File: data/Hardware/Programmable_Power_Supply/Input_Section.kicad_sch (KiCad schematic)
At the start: 20 parts, among them J1 Barrel_Jack_MountingPin, Q1 BSC050N03LS_G, Q2 2N7002, U2 TPS26631PWP, U3 TPS54202DDC

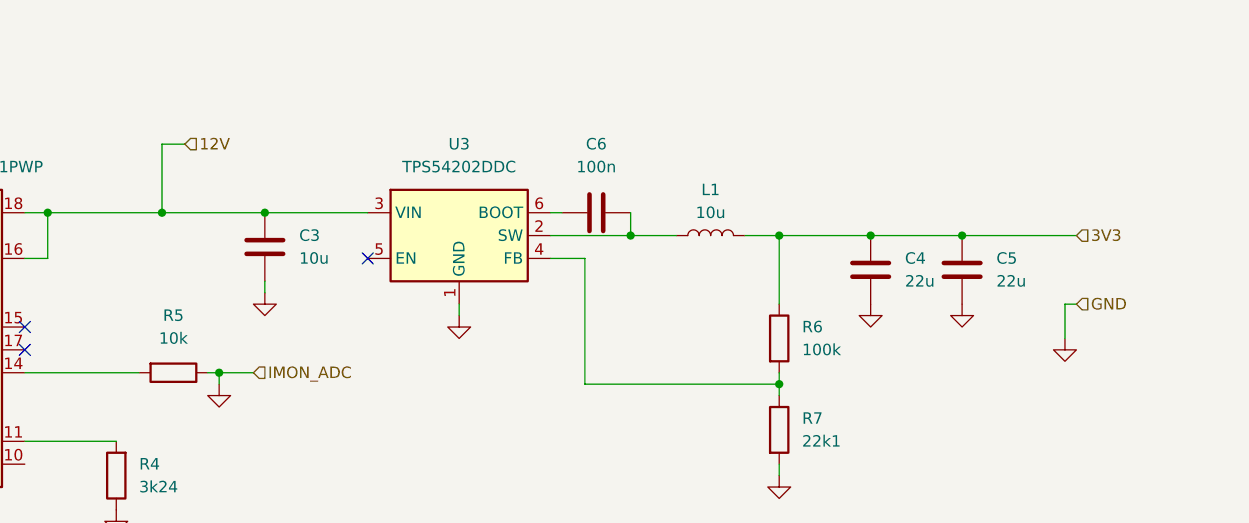
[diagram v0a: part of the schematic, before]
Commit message: feat: Adding output section to the schematic.
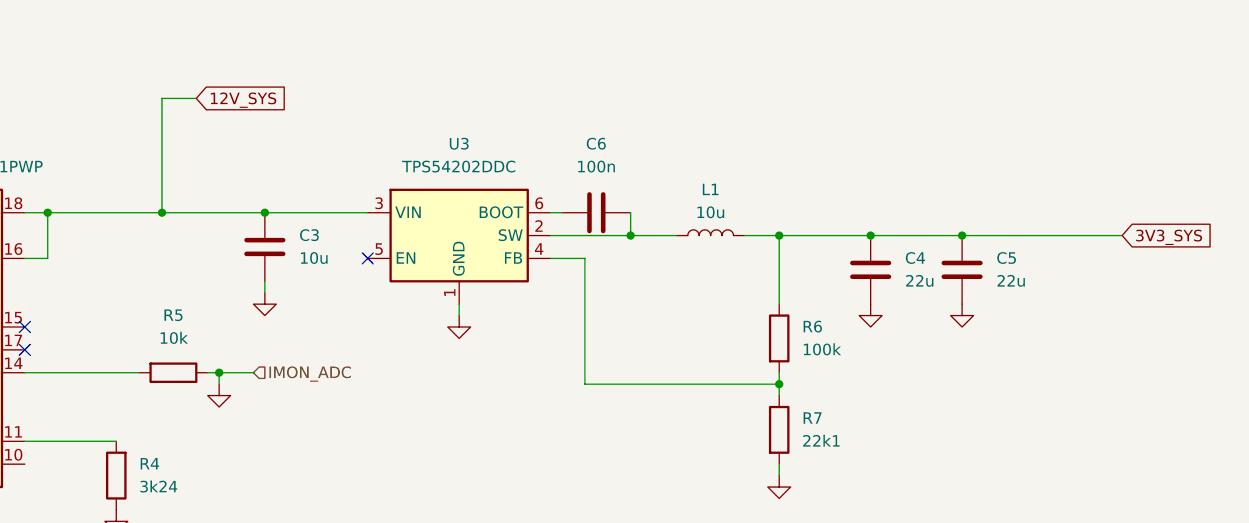
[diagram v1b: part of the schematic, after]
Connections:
- net 12V renamed 12V_SYS
- net 3V3 renamed 3V3_SYS
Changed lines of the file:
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@@
+	(wire
+		(pts
+			(xy 151.13 50.8) (xy 154.94 50.8)
+		)
+		(stroke
+			(width 0)
+			(type default)
+		)
+	)
 	(wire
 		(pts
@@
 	(wire
 		(pts
-			(xy 251.46 73.66) (xy 251.46 77.47)
-		)
-		(stroke
-			(width 0)
-			(type default)
-		)
-	)
-	(wire
-		(pts
 			(xy 63.5 49.53) (xy 76.2 49.53)
 		)
@@
 	(wire
 		(pts
-			(xy 153.67 55.88) (xy 151.13 55.88)
-		)
-		(stroke
-			(width 0)
-			(type default)
-		)
-	)
-	(wire
-		(pts
 			(xy 198.12 82.55) (xy 219.71 82.55)
 		)
@@
 	(wire
 		(pts
-			(xy 240.03 66.04) (xy 252.73 66.04)
+			(xy 240.03 66.04) (xy 257.81 66.04)
 		)
 		(stroke
@@
 	(wire
 		(pts
-			(xy 151.13 55.88) (xy 151.13 63.5)
-		)
-		(stroke
-			(width 0)
-			(type default)
-		)
-	)
-	(wire
-		(pts
 			(xy 76.2 83.82) (xy 76.2 90.17)
 		)
@@
 	(wire
 		(pts
-			(xy 252.73 73.66) (xy 251.46 73.66)
-		)
-		(stroke
-			(width 0)
-			(type default)
-		)
-	)
-	(wire
-		(pts
 			(xy 53.34 49.53) (xy 63.5 49.53)
 		)
@@
 	(wire
 		(pts
+			(xy 151.13 50.8) (xy 151.13 63.5)
+		)
+		(stroke
+			(width 0)
+			(type default)
+		)
+	)
+	(wire
+		(pts
 			(xy 88.9 83.82) (xy 76.2 83.82)
 		)
@@
 		)
 	)
-	(hierarchical_label "12V"
+	(global_label "3V3_SYS"
 		(shape input)
-		(at 153.67 55.88 0)
+		(at 257.81 66.04 0)
+		(fields_autoplaced yes)
 		(effects
 			(font
@@
 			(justify left)
 		)
-	)
-	(hierarchical_label "GND"
+		(property "Intersheetrefs" "${INTERSHEET_REFS}"
+			(at 268.778 66.04 0)
+			(effects
+				(font
+					(size 1.27 1.27)
+				)
+				(justify left)
+				(hide yes)
+			)
+		)
+	)
+	(global_label "12V_SYS"
 		(shape input)
-		(at 252.73 73.66 0)
+		(at 154.94 50.8 0)
+		(fields_autoplaced yes)
 		(effects
 			(font
@@
 			)
 			(justify left)
+		)
+		(property "Intersheetrefs" "${INTERSHEET_REFS}"
+			(at 165.908 50.8 0)
+			(effects
+				(font
+					(size 1.27 1.27)
+				)
+				(justify left)
+				(hide yes)
+			)
 		)
 	)
@@
 		)
 	)
-	(hierarchical_label "3V3"
-		(shape input)
-		(at 252.73 66.04 0)
-		(effects
-			(font
-				(size 1.27 1.27)
-			)
-			(justify left)
-		)
-	)
 	(symbol
 		(lib_id "power:GND")
@@
 					(unit 1)
 				)
-			)
-		)
-	)
-	(symbol
-		(lib_id "power:GND")
-		(at 251.46 77.47 0)
-		(unit 1)
-		(exclude_from_sim no)
-		(in_bom yes)
-		(on_board yes)
-		(dnp no)
-		(fields_autoplaced yes)
-		(property "Reference" "#PWR03"
-			(at 251.46 83.82 0)
-			(effects
-				(font
-					(size 1.27 1.27)
-				)
-				(hide yes)
-			)
-		)
-		(property "Value" "GND"
-			(at 251.46 82.55 0)
-			(effects
-				(font
-					(size 1.27 1.27)
-				)
-				(hide yes)
-			)
-		)
-		(property "Footprint" ""
-			(at 251.46 77.47 0)
-			(effects
-				(font
-					(size 1.27 1.27)
-				)
-				(hide yes)
-			)
-		)
-		(property "Datasheet" ""
-			(at 251.46 77.47 0)
-			(effects
-				(font
-					(size 1.27 1.27)
-				)
-				(hide yes)
-			)
-		)
-		(property "Description" "Power symbol creates a global label with name \"GND\" , ground"
-			(at 251.46 77.47 0)
-			(effects
-				(font
-					(size 1.27 1.27)
-				)
-				(hide yes)
-			)
-		)
-		(pin "1"
-		)
-		(instances
-			(project "Programmable_Power_Supply"
-				(path "/b54e5edd-9bd1-4c5e-a8c2-662f0aedeac0/0d4dc9d8-4ae1-4f7b-b0fe-cdea114c506b"
-					(reference "#PWR03")
-					(unit 1)
-				)

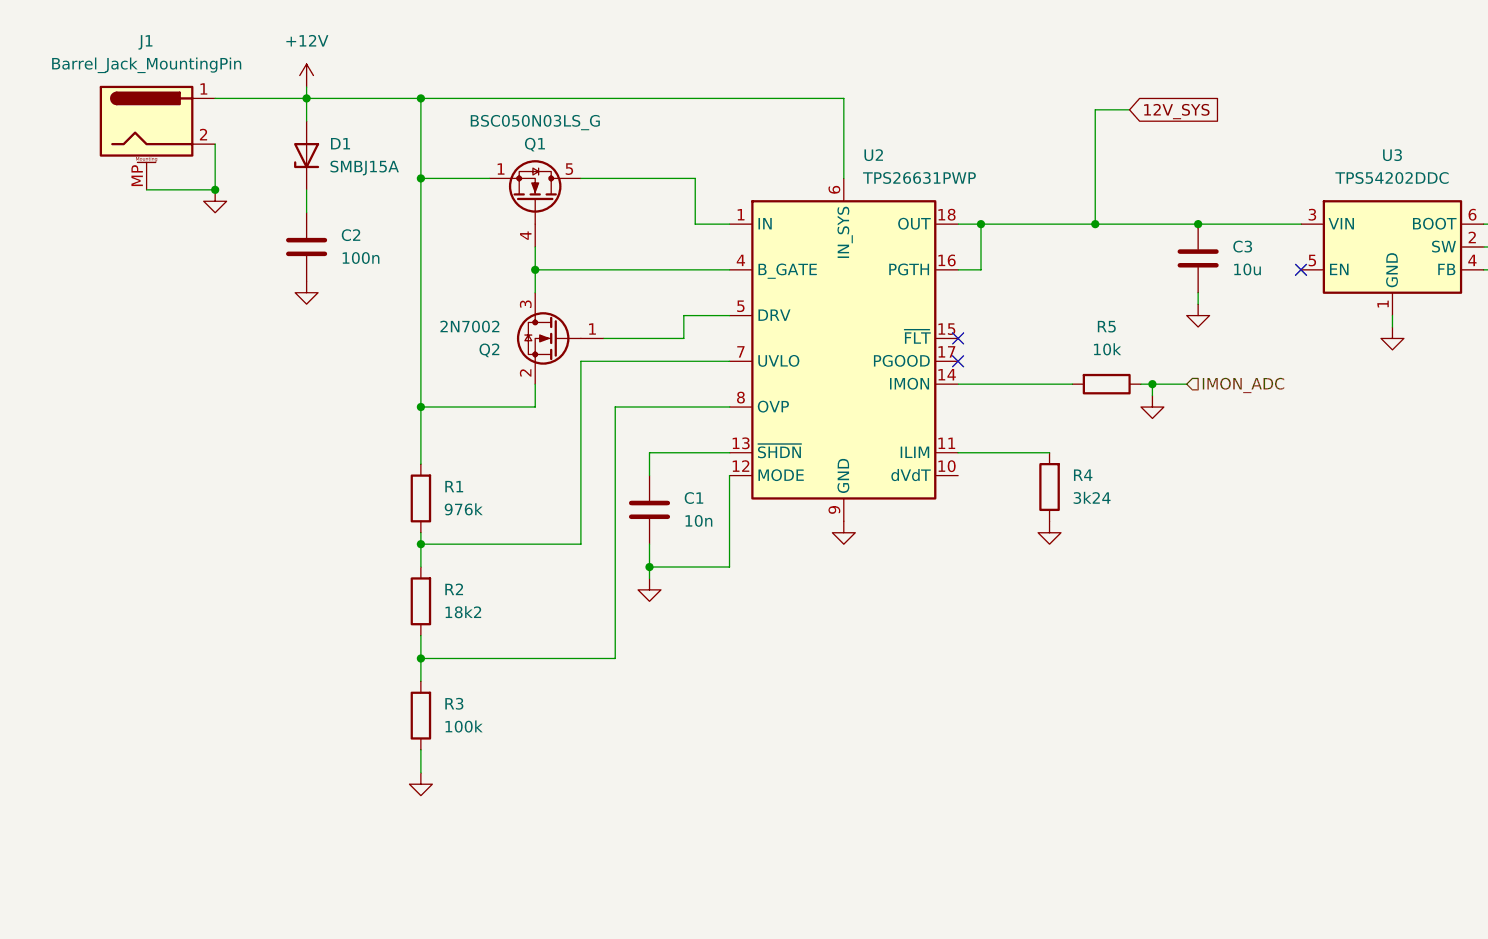
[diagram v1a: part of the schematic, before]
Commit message: feat: First draw of full schematic with all footprints and symbols.
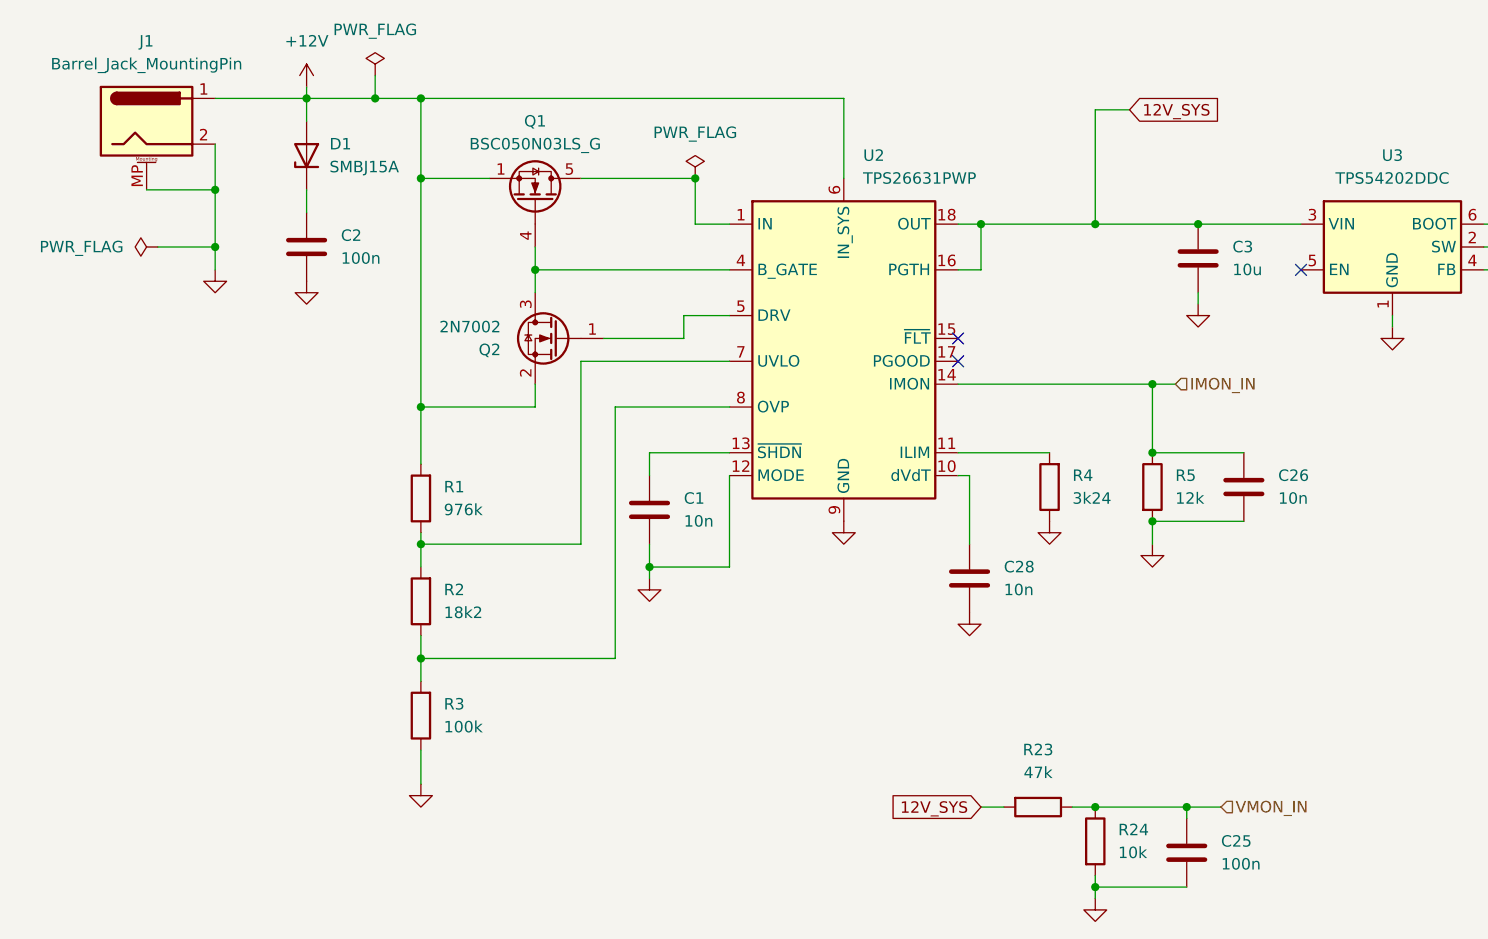
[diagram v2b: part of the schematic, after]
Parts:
- added C25: 100n, Capacitor_SMD:C_0805_2012Metric_Pad1.18x1.45mm_HandSolder, symbol Device:C
- added C26, C28: 10n, Capacitor_SMD:C_0805_2012Metric_Pad1.18x1.45mm_HandSolder, symbol Device:C
- added R23: 47k, Resistor_SMD:R_0603_1608Metric_Pad0.98x0.95mm_HandSolder, symbol Device:R
- added R24: 10k, Resistor_SMD:R_0603_1608Metric_Pad0.98x0.95mm_HandSolder, symbol Device:R
- C1: footprint (none) -> Capacitor_SMD:C_0201_0603Metric_Pad0.64x0.40mm_HandSolder
- C2, C6: footprint (none) -> Capacitor_SMD:C_0805_2012Metric_Pad1.18x1.45mm_HandSolder
- C3, C4, C5: footprint (none) -> Capacitor_SMD:C_1206_3216Metric_Pad1.33x1.80mm_HandSolder
- L1: footprint (none) -> Inductor_SMD:L_Taiyo-Yuden_NR-60xx_HandSoldering
- R1, R2, R3, R4, R6, R7: footprint (none) -> Resistor_SMD:R_0603_1608Metric_Pad0.98x0.95mm_HandSolder
- R5: value 10k -> 12k; footprint (none) -> Resistor_SMD:R_0603_1608Metric_Pad0.98x0.95mm_HandSolder
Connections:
- net +12V: now also Q1.2 (S), Q1.3 (S)
- net 12V_SYS: now also R23.2
- net GND: now also R5.2, C25.2, C26.2, C28.2, R24.2; no longer R5.1
- net at Q1.5 (D), U2.1 (IN), U2.2 (IN)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: now also Q1.6 (D), Q1.7 (D), Q1.8 (D)
- net at U2.10 (dVdT): now also C28.1
- net IMON_IN: now reaches U2.14 (IMON)
- net IMON_IN: now also R5.1, C26.1; no longer R5.2
- new net VMON_IN: C25.1, R23.1, R24.1
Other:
- moved on the sheet: R5

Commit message: feat: Final version of revision A of the schematic with mouser product numbers attached.
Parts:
- removed C26: 10n, Capacitor_SMD:C_0805_2012Metric_Pad1.18x1.45mm_HandSolder, symbol Device:C
- added C12: 10n, Capacitor_SMD:C_0201_0603Metric_Pad0.64x0.40mm_HandSolder, symbol Device:C
- C1: Mouser (none) -> MLASU063SB5103KFNA01
- C2, C25, C6: footprint Capacitor_SMD:C_0805_2012Metric_Pad1.18x1.45mm_HandSolder -> Capacitor_SMD:C_0201_0603Metric_Pad0.64x0.40mm_HandSolder; Mouser (none) -> MLASG063SB5104KFNA01
- C28: footprint Capacitor_SMD:C_0805_2012Metric_Pad1.18x1.45mm_HandSolder -> Capacitor_SMD:C_0201_0603Metric_Pad0.64x0.40mm_HandSolder; Mouser (none) -> MLASU063SB5103KFNA01
- C3: Mouser (none) -> GXT31CR6YA106KE01L
- C4, C5: Mouser (none) -> GRM31CC71C226ME11K
- D1: Mouser (none) -> SMBJ15A
- J1: footprint Connector_BarrelJack:BarrelJack_CUI_PJ-102AH_Horizontal -> Connector_BarrelJack:BarrelJack_CUI_PJ-063AH_Horizontal; Mouser (none) -> PJ-063AH
- L1: value 10u -> 10uH; footprint Inductor_SMD:L_Taiyo-Yuden_NR-60xx_HandSoldering -> Szymon_Piorun_Library:SRP6540; Mouser (none) -> SRP6540-100M
- Q1: footprint Package_SON:Infineon_PG-TDSON-8_6.15x5.15mm -> Szymon_Piorun_Library:Infineon_PG-TDSON-8_6.15x5.15mm; Mouser (none) -> BSC030N03LS G
- Q2: Mouser (none) -> 2N7002
- R1: Mouser (none) -> CRCW0603976KFKTA
- R2: Mouser (none) -> AF0603FR-0718K2L
- R23: Mouser (none) -> CRCW060347K0FKECC
- R24: Mouser (none) -> RCA060310K0FKEC
- R3, R6: Mouser (none) -> RCA0603100KFKEC
- R4: value 3k24 -> 3k3; Mouser (none) -> CR0603-FX-3301ELF
- R5: Mouser (none) -> 560112116040
- R7: Mouser (none) -> CRCW060322K1FKEBC
- U2: footprint Package_SO:HTSSOP-20-1EP_4.4x6.5mm_P0.65mm_EP3.4x6.5mm_Mask2.96x2.96mm_ThermalVias -> Szymon_Piorun_Library:HTSSOP-20-1EP_4.4x6.5mm_P0.65mm_EP3.4x6.5mm_Mask2.96x2.96mm_ThermalVias; Mouser (none) -> TPS26633PWPR
- U3: Mouser (none) -> TPS542025DDCR
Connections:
- net GND: now also R3.2, C12.2; no longer R3.1
- net IMON_IN: now also C12.1
- net at R2.1, U2.8 (OVP): now also R3.1; no longer R3.2

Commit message: feat: First full layout of the PCB
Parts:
- J1: value Barrel_Jack_MountingPin -> Barrel Jack Input Port
- Q1: Mouser BSC030N03LS G -> (none)
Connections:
- net +12V: now also C2.1
- net GND: now also D1.1 (K)
- net TPS_OVP: now reaches R2.1, R3.1, U2.8 (OVP)
- net TPS_UVLO: now reaches R1.1, R2.2, U2.7 (UVLO)
- net TPS_12V: now reaches Q1.5 (D), U2.1 (IN), U2.2 (IN), U2.3 (IN)
- net TPS_12V: no longer Q1.6 (D), Q1.7 (D), Q1.8 (D)
- net TPS_B_GATE: now reaches Q1.4 (G), Q2.3 (D), U2.4 (B_GATE)
- net TPS_DRV: now reaches Q2.1 (G), U2.5 (DRV)
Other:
- note added: "Input Voltage Monitor"
- moved on the sheet: C1, C12, C2, C25, C28, C3, C4, C5, C6, D1, J1, L1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
